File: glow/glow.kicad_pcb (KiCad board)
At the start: 2 copper layers, 97 x 99.4 mm, 59 parts, among them J1 Conn_01x04_Female, J2 Conn_01x05_Female, J3 Conn_01x03_Female, J4 Conn_01x06_Female, J5 Conn_01x03_Female, SW8 SW_Push

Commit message: routing
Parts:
- removed SW8: SW_Push, custom:SW_MX_reversible
- added H1: M4, MountingHole:MountingHole_4mm_Pad_Via, F.Cu at (234.0, 105.5)
- added H2: M4, MountingHole:MountingHole_4mm_Pad_Via, F.Cu at (234.0, 75.5)
- added kibuzzard-61F01B61: G***, kibuzzard-61F01B61, F.Cu at (234.5, 98.0)
- added kibuzzard-6208EFFE: G***, kibuzzard-6208EFFE, B.Cu at (234.1, 98.2)
- J3: value Conn_01x03_Female -> In
- J5: value Conn_01x03_Female -> Out
- moved D26 187.0 mm to (271.0, 82.2), turned to -45 degrees
- moved D56 78.6 mm to (191.0, 141.8), turned to 60 degrees
- moved D25 3.40 mm to (271.0, 82.2), turned to -45 degrees
- moved R1 3.28 mm to (195.2, 100.0), turned to 90 degrees
- moved R2 3.26 mm to (195.3, 100.0), turned to 90 degrees
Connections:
- D21 pad 2: Gnd -> Net-(D21-Pad2)
- D21 pad 4: Vcc -> Net-(D21-Pad4)
- D22 pad 2: Gnd -> Net-(D22-Pad2)
- D22 pad 4: Vcc -> Net-(D22-Pad4)
- D23 pad 2: Gnd -> Net-(D21-Pad2)
- D23 pad 4: Vcc -> Net-(D21-Pad4)
- D24 pad 2: Gnd -> Net-(D22-Pad2)
- D24 pad 4: Vcc -> Net-(D22-Pad4)
- D25 pad 2: Gnd -> Net-(D21-Pad2)
- D25 pad 4: Vcc -> Net-(D21-Pad4)
- D26 pad 2: Gnd -> Net-(D22-Pad2)
- D26 pad 4: Vcc -> Net-(D22-Pad4)
- D33 pad 4: Vcc -> Net-(D33-Pad4)
- D34 pad 1: Net-(D21-Pad3) -> unconnected-(D34-Pad1)
- D37 pad 2: Gnd -> Net-(D21-Pad2)
- D37 pad 4: Vcc -> Net-(D21-Pad4)
- D38 pad 2: Gnd -> Net-(D22-Pad2)
- D38 pad 4: Vcc -> Net-(D22-Pad4)
- D39 pad 2: Gnd -> Net-(D21-Pad2)
- D39 pad 4: Vcc -> Net-(D21-Pad4)
- D40 pad 2: Gnd -> Net-(D22-Pad2)
- D40 pad 4: Vcc -> Net-(D22-Pad4)
- D41 pad 2: Gnd -> Net-(D21-Pad2)
- D41 pad 4: Vcc -> Net-(D21-Pad4)
- D42 pad 1: Net-(D41-Pad1) -> Net-(D42-Pad1)
- D42 pad 2: Gnd -> Net-(D22-Pad2)
- D42 pad 4: Vcc -> Net-(D22-Pad4)
- D47 pad 2: Gnd -> Net-(D21-Pad2)
- D47 pad 4: Vcc -> Net-(D47-Pad4)
- D48 pad 2: Gnd -> Net-(D48-Pad2)
- D48 pad 3: Net-(D41-Pad1) -> Net-(D42-Pad1)
- D48 pad 4: Vcc -> Net-(D48-Pad4)
- D49 pad 2: Gnd -> Net-(D21-Pad2)
- D49 pad 4: Vcc -> Net-(D47-Pad4)
- D5 pad 4: Vcc -> Net-(D33-Pad4)
- D50 pad 2: Gnd -> Net-(D48-Pad2)
- D50 pad 4: Vcc -> Net-(D48-Pad4)
- D51 pad 2: Gnd -> Net-(D21-Pad2)
- D51 pad 4: Vcc -> Net-(D47-Pad4)
- D52 pad 2: Gnd -> Net-(D48-Pad2)
- D52 pad 4: Vcc -> Net-(D48-Pad4)
- D55 pad 2: Gnd -> Net-(D55-Pad2)
- D55 pad 4: Vcc -> Net-(D47-Pad4)
- D56 pad 2: Gnd -> Net-(D48-Pad2)
- D56 pad 4: Vcc -> Net-(D48-Pad4)
- D57 pad 2: Gnd -> Net-(D55-Pad2)
- D57 pad 4: Vcc -> Net-(D47-Pad4)
- D58 pad 2: Gnd -> Net-(D48-Pad2)
- D58 pad 4: Vcc -> Net-(D48-Pad4)
- D59 pad 2: Gnd -> Net-(D55-Pad2)
- D59 pad 4: Vcc -> Net-(D47-Pad4)
- D60 pad 2: Gnd -> Net-(D48-Pad2)
- D60 pad 4: Vcc -> Net-(D48-Pad4)
- D7 pad 4: Vcc -> Net-(D33-Pad4)
- R1 pad 2: Net-(D5-Pad3) -> Net-(R1-Pad2)
- R2 pad 2: Net-(D5-Pad3) -> Net-(R1-Pad2)
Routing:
- net Gnd: track 2.76 -> 433.4 mm, vias 0 -> 16
- net Vcc: track 2.92 -> 410.0 mm, vias 0 -> 16
- net Dout: track 0.00 -> 168.6 mm, vias 0 -> 1
- net Net-(D23-Pad1): track 17.0 -> 32.2 mm, vias 0 -> 2
- net Net-(D51-Pad1): track 14.0 -> 24.2 mm, vias 0 -> 2
- net Net-(D37-Pad1): track 11.5 -> 21.5 mm, vias 0 -> 2
- net Net-(D39-Pad1): track 16.0 -> 25.7 mm, vias 0 -> 2
- net Net-(D55-Pad1): track 13.1 -> 22.6 mm, vias 0 -> 2
- net Net-(D49-Pad1): track 16.0 -> 25.4 mm, vias 0 -> 2
- net Net-(D33-Pad3): track 13.4 -> 22.5 mm, vias 0 -> 2
- net Net-(D21-Pad1): track 18.5 -> 26.6 mm, vias 0 -> 2
- net Net-(R1-Pad2): track 0.00 -> 8.01 mm, vias 0 -> 1
- net Net-(D5-Pad3): track 7.99 -> 0.00 mm
- net Net-(D21-Pad3): track 21.0 -> 28.9 mm, vias 0 -> 2
- net Net-(D57-Pad1): track 12.8 -> 20.7 mm, vias 0 -> 2
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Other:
- outline, holes or cut-outs redrawn
- board text added: "5V"
- board text added: "DIN"
- board text added: "Do"
- board text added: "GND"

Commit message: routing, logos
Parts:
- removed D11, D12, D13, D14, D15, D16, D17, D19, D20, D27, D31, D32, D35, D36, D9: D, custom:Diode_TH_SOD123
- removed the G*** at (93.2, 129.1)
- removed the G*** at (234.0, 89.0)
- removed the G*** at (93.3, 129.0)
- removed the G*** at (234.1, 89.0)
- removed J1: Conn_01x04_Female, Connector_PinHeader_2.54mm:PinHeader_1x04_P2.54mm_Vertical
- removed J2: Conn_01x05_Female, customs:PinHeader_1x05_P2.54mm_Vertical
- removed J4: Conn_01x06_Female, Connector_PinHeader_2.54mm:PinHeader_1x06_P2.54mm_Vertical
- added G***: LOGO, LOGO, B.Cu at (86.3, 70.3)
- added G***: LOGO, LOGO, B.Cu at (86.3, 70.1)
- moved kibuzzard-61F01B61 169.6 mm to (73.8, 43.5)
- moved kibuzzard-6208EFFE 169.6 mm to (73.5, 43.6)
- moved C1 149.1 mm to (52.0, 77.3)
- moved C2 149.1 mm to (52.0, 77.3)
- moved D21 149.1 mm to (86.8, 42.1)
- moved D22 149.1 mm to (86.8, 42.1)
- moved D23 149.1 mm to (110.5, 42.8)
- moved D24 149.1 mm to (110.5, 42.8)
- moved D25 149.1 mm to (123.3, 62.3)
- moved D26 149.1 mm to (123.3, 62.3)
- moved D33 149.1 mm to (61.5, 43.8)
- moved D34 149.1 mm to (61.5, 43.8)
- moved D37 149.1 mm to (126.8, 87.8)
- moved D38 149.1 mm to (126.8, 87.8)
- moved D39 149.1 mm to (115.3, 97.3)
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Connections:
- D21 pad 2: Net-(D21-Pad2) -> Gnd
- D21 pad 3: Net-(D21-Pad3) -> Net-(D34-Pad1)
- D21 pad 4: Net-(D21-Pad4) -> Vcc
- D22 pad 2: Net-(D22-Pad2) -> Gnd
- D22 pad 3: Net-(D21-Pad3) -> Net-(D34-Pad1)
- D22 pad 4: Net-(D22-Pad4) -> Vcc
- D23 pad 2: Net-(D21-Pad2) -> Gnd
- D23 pad 4: Net-(D21-Pad4) -> Vcc
- D24 pad 2: Net-(D22-Pad2) -> Gnd
- D24 pad 4: Net-(D22-Pad4) -> Vcc
- D25 pad 2: Net-(D21-Pad2) -> Gnd
- D25 pad 4: Net-(D21-Pad4) -> Vcc
- D26 pad 2: Net-(D22-Pad2) -> Gnd
- D26 pad 4: Net-(D22-Pad4) -> Vcc
- D33 pad 1: Net-(D21-Pad3) -> Net-(D34-Pad1)
- D33 pad 4: Net-(D33-Pad4) -> Vcc
- D34 pad 1: unconnected-(D34-Pad1) -> Net-(D34-Pad1)
- D37 pad 2: Net-(D21-Pad2) -> Gnd
- D37 pad 4: Net-(D21-Pad4) -> Vcc
- D38 pad 2: Net-(D22-Pad2) -> Gnd
- D38 pad 4: Net-(D22-Pad4) -> Vcc
- D39 pad 2: Net-(D21-Pad2) -> Gnd
- D39 pad 4: Net-(D21-Pad4) -> Vcc
- D40 pad 2: Net-(D22-Pad2) -> Gnd
- D40 pad 4: Net-(D22-Pad4) -> Vcc
- D41 pad 2: Net-(D21-Pad2) -> Gnd
- D41 pad 4: Net-(D21-Pad4) -> Vcc
- D42 pad 1: Net-(D42-Pad1) -> Net-(D41-Pad1)
- D42 pad 2: Net-(D22-Pad2) -> Gnd
- D42 pad 4: Net-(D22-Pad4) -> Vcc
- D47 pad 2: Net-(D21-Pad2) -> Gnd
- D47 pad 4: Net-(D47-Pad4) -> Vcc
- D48 pad 2: Net-(D48-Pad2) -> Gnd
- D48 pad 3: Net-(D42-Pad1) -> Net-(D41-Pad1)
- D48 pad 4: Net-(D48-Pad4) -> Vcc
- D49 pad 2: Net-(D21-Pad2) -> Gnd
- D49 pad 4: Net-(D47-Pad4) -> Vcc
- D5 pad 3: Net-(D5-Pad3) -> Net-(R1-Pad2)
- D5 pad 4: Net-(D33-Pad4) -> Vcc
- D50 pad 2: Net-(D48-Pad2) -> Gnd
- D50 pad 4: Net-(D48-Pad4) -> Vcc
- D51 pad 2: Net-(D21-Pad2) -> Gnd
- D51 pad 4: Net-(D47-Pad4) -> Vcc
- D52 pad 2: Net-(D48-Pad2) -> Gnd
- D52 pad 4: Net-(D48-Pad4) -> Vcc
- D55 pad 2: Net-(D55-Pad2) -> Gnd
- D55 pad 4: Net-(D47-Pad4) -> Vcc
- D56 pad 2: Net-(D48-Pad2) -> Gnd
- D56 pad 4: Net-(D48-Pad4) -> Vcc
- D57 pad 2: Net-(D55-Pad2) -> Gnd
- D57 pad 4: Net-(D47-Pad4) -> Vcc
- D58 pad 2: Net-(D48-Pad2) -> Gnd
- D58 pad 4: Net-(D48-Pad4) -> Vcc
- D59 pad 2: Net-(D55-Pad2) -> Gnd
- D59 pad 4: Net-(D47-Pad4) -> Vcc
- D6 pad 3: Net-(D5-Pad3) -> Net-(R1-Pad2)
- D60 pad 2: Net-(D48-Pad2) -> Gnd
- D60 pad 4: Net-(D48-Pad4) -> Vcc
- D7 pad 4: Net-(D33-Pad4) -> Vcc
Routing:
- net Net-(D34-Pad1): track 0.00 -> 28.9 mm, vias 0 -> 2
- net Net-(D21-Pad3): track 28.9 -> 0.00 mm, vias 2 -> 0
- net Net-(D5-Pad1): track 15.3 -> 21.5 mm, vias 1 -> 2
- net Vcc: track 410.0 -> 406.6 mm
- net Net-(R1-Pad2): track 8.01 -> 11.4 mm, vias 1 -> 2
- net Gnd: track 433.4 -> 430.5 mm
- net Dout: track 168.6 -> 167.9 mm
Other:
- board text added: "C"
- board text added: "CNANO RGB BOT PLATE"
- board text added: "DOUT"
- board text added: "R"
- board text added: "REV1.0"
- board text removed: "Do"

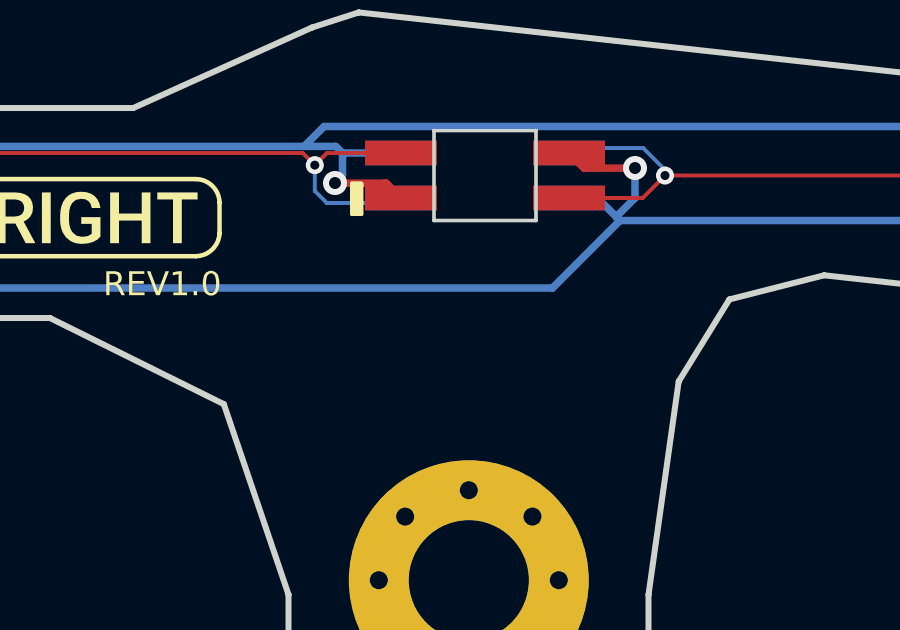
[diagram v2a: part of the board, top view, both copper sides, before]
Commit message: add license
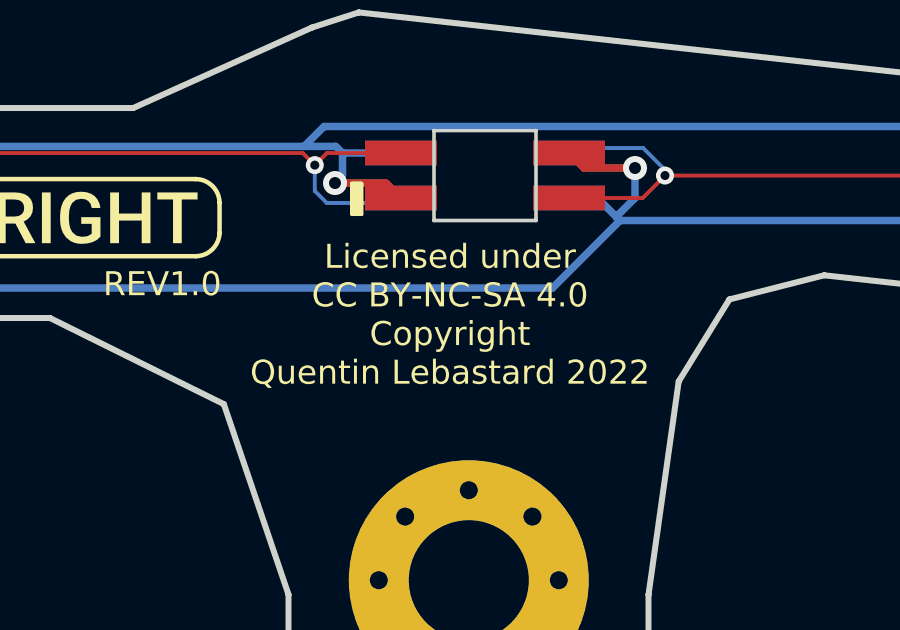
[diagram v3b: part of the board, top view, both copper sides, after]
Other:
- board text added: "Licensed under CC BY-NC-SA 4.0 Copyright Quentin Lebastard 2022"
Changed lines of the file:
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@@
     (effects (font (size 0.8 0.8) (thickness 0.15)) (justify mirror))
+  )
+  (gr_text "Licensed under \nCC BY-NC-SA 4.0\nCopyright \nQuentin Lebastard 2022" (at 85.6 46.75) (layer "B.SilkS")
+    (effects (font (size 0.8 0.8) (thickness 0.12)) (justify mirror))
   )
   (gr_text "R" (at 47.5 80.2) (layer "B.SilkS")
@@
     (effects (font (size 0.8 0.8) (thickness 0.15)) (justify left))
   )
+  (gr_text "Licensed under \nCC BY-NC-SA 4.0\nCopyright \nQuentin Lebastard 2022" (at 85.590546 46.718756) (layer "F.SilkS")
+    (effects (font (size 0.8 0.8) (thickness 0.12)))
+  )
   (gr_text "CNANO RGB\nBOT PLATE" (at 86.1 62.4) (layer "F.SilkS")
